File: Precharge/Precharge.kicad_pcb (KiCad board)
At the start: 2 copper layers, 87.1 x 86.1 mm, 62 parts, among them J1 Conn_01x02, J2 Conn_01x02, J3 Molex MicroFit, J4 Conn_02x03_Counter_Clockwise, K1 KT12-1A-40L-THT, Q1 AO3400A, Q2 2N7002, U1 LM393, U2 4N35, U3 4N35, U4 NE555D

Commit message: v2.0
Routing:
- net GLV-: vias 28 -> 29
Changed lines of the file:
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@@
 	)
 	(via
+		(at 154.432 62.23)
+		(size 0.6)
+		(drill 0.3)
+		(layers "F.Cu" "B.Cu")
+		(free yes)
+		(net 2)
+	)
+	(via
 		(at 145.754 96.239)
 		(size 0.6)
@@
 	)
 	(via
-		(at 133.154 107.739)
+		(at 133.096 106.426)
 		(size 0.6)
 		(drill 0.3)
@@
 	)
 	(via
-		(at 133.279 105.989)
+		(at 133.279 100.33)
 		(size 0.6)
 		(drill 0.3)
@@
 	)
 	(segment
-		(start 117.9576 84.5926)
+		(start 117.379 84.014)
 		(end 116.673 83.308)
 		(width 0.635)
@@
 	)
 	(segment
-		(start 117.9576 102.2604)
-		(end 117.9576 84.5926)
-		(width 0.635)
-		(layer "F.Cu")
-		(net 36)
-	)
-	(segment
 		(start 113.03 79.315)
 		(end 112.979 79.264)
@@
 	(segment
 		(start 117.348 102.87)
-		(end 117.9576 102.2604)
+		(end 117.379 102.839)
 		(width 0.635)
 		(layer "F.Cu")
@@
 	)
 	(segment
+		(start 117.379 102.839)
+		(end 117.379 84.014)
+		(width 0.635)
+		(layer "F.Cu")
+		(net 36)
+	)
+	(segment
 		(start 74.1172 92.1512)
 		(end 74.1172 72.4408)
@@
 		(polygon
 			(pts
-				(xy 157.229 51.239) (xy 133.204 51.439) (xy 132.779 137.489) (xy 157.229 137.464)
+				(xy 156.467 58.859) (xy 131.813 58.984) (xy 131.763 128.345) (xy 156.467 128.32)
 			)
 		)

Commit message: v2.1
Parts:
- added Q3: 2N7002, Package_TO_SOT_SMD:SOT-23, F.Cu at (139.0, 96.3)
- added R29: 1M, Resistor_SMD:R_0603_1608Metric_Pad0.98x0.95mm_HandSolder, F.Cu at (150.1, 89.2)
- R8: value 120 -> 150
- moved R26 13.8 mm to (138.2, 85.0), turned to -90 degrees
- moved R27 8.28 mm to (138.5, 91.2), turned to 90 degrees
- moved R27 7.57 mm to (147.8, 84.9), turned to 90 degrees
- moved R23 5.09 mm to (132.6, 84.8)
- moved C2 4.18 mm to (145.8, 84.9)
- moved R24 4.10 mm to (143.9, 84.9)
- moved R28 4.09 mm to (150.1, 84.9), turned to 90 degrees
- moved C5 1.96 mm to (150.1, 93.2)
- moved G*** 1.59 mm to (109.6, 133.3)
- moved Q1 1.23 mm to (149.6, 98.2), turned to 90 degrees
- moved Q2 0.81 mm to (135.4, 84.6)
- moved R25 0.30 mm to (140.0, 84.9), turned to 90 degrees
- moved R22 0.11 mm to (141.8, 85.0), turned to -90 degrees
- renumbered D7 to D1, D1 to D2, D2 to D3, D6 to D4, D3 to D5, D5 to D6, D4 to D7, R28 to R18, R29 to R19, R18 to R20, R19 to R21, R20 to R22, R21 to R23, R22 to R24, R23 to R25, R24 to R26, R25 to R27, R26 to R28
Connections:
- net Net-(R15-Pad2) renamed /Precharge_12V
- C2 pad 2: GLV- -> Net-(Q3-D)
- C3 pad 2: GLV- -> Net-(Q3-D)
- C4 pad 2: GLV- -> Net-(Q3-D)
- C5 pad 2: GLV- -> Net-(Q3-D)
- R24 pad 1: GLV- -> Net-(Q3-D)
- U1 pad 5: unconnected-(U1B-+-Pad5) -> (no net)
- U1 pad 6: unconnected-(U1B---Pad6) -> (no net)
- U1 pad 7: unconnected-(U1-Pad7) -> (no net)
- U4 pad 1: GLV- -> Net-(Q3-D)
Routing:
- net HV-: track 110.8 -> 194.4 mm, vias 150 -> 217
- net Net-(Q3-D): track 0.00 -> 45.9 mm
- net /Precharge_12V: track 6.34 -> 34.3 mm, vias 0 -> 1
- net /PreCh_Int: track 47.4 -> 67.4 mm, vias 3 -> 2
- net Net-(U4-DIS): track 28.6 -> 15.9 mm
- net Net-(D2-A): track 20.0 -> 9.80 mm
- net /AIR+_Con: track 87.9 -> 81.7 mm
- net Net-(D4-A): track 31.7 -> 26.3 mm
- net GLV-: track 0.26 -> 5.23 mm, vias 29 -> 38
- net /PreCh_Complt: track 61.3 -> 65.1 mm
- net /SDC_IN: track 116.0 -> 113.1 mm, vias 2 -> 0
- net Net-(U4-TR): track 11.3 -> 12.7 mm
- net Net-(U1C-V+): track 17.2 -> 16.0 mm
- net Net-(J2-Pin_2): track 54.7 -> 55.8 mm
- net /AIR+: track 83.3 -> 82.4 mm
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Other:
- board size 87.1 x 86.1 mm -> 85 x 85 mm
- board text added: "0.2000 mm / 0.2000 mm"
- board text added: "0.3000 mm"
- board text added: "1.6000 mm"
- board text added: "2"
- board text added: "85.0372 mm x 85.0344 mm"
- board text added: "BOARD CHARACTERISTICS"
- board text added: "Board Thickness:"
- board text added: "Board overall dimensions:"
- board text added: "Castellated pads:"
- board text added: "Copper Finish:"
- board text added: "Copper Layer Count:"
- board text added: "Edge card connectors:"
- board text added: "Impedance Control:"
- board text added: "Min hole diameter:"
- board text added: "Min track/spacing:"
- board text added: "No"
- board text added: "None"
- board text added: "Plated Board Edge:"
- board text added: "v2.1"
- board text removed: "v2.0"

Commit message: v2.1
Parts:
- Q3: value 2N7002 -> AO3400A
- R27: value 1M -> 10K
- moved D6 5.03 mm to (144.6, 71.2)
- moved D7 4.97 mm to (139.6, 71.1)
- moved REF** 0.20 mm to (84.8, 76.1)
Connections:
- net Net-(U1-Pad1) renamed /Comp_Out
- R27 pad 1: Net-(U4-DIS) -> /SDC_IN
- R27 pad 2: GLV- -> Net-(U4-TR)
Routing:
- net /SDC_IN: track 113.1 -> 119.1 mm
- net /AIR+_Con: track 81.7 -> 78.3 mm
- net Net-(U4-DIS): track 15.9 -> 12.9 mm
- net Net-(U4-TR): track 12.7 -> 15.5 mm
- net Net-(D4-A): track 26.3 -> 29.0 mm
- net Net-(D3-A): track 7.97 -> 6.23 mm
- net Net-(Q3-D): track 45.9 -> 44.9 mm
- net GLV-: vias 38 -> 37

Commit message: v3.0 coming up
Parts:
- removed C3: 0.01uF, Capacitor_SMD:C_0603_1608Metric_Pad1.08x0.95mm_HandSolder
- removed C4: 0.1uF, Capacitor_SMD:C_0603_1608Metric_Pad1.08x0.95mm_HandSolder
- removed C5: 10uF, Resistor_SMD:R_0805_2012Metric_Pad1.20x1.40mm_HandSolder
- removed D7: 1N5819, Diode_THT:D_DO-41_SOD81_P7.62mm_Horizontal
- removed R24, R29: 1M, Resistor_SMD:R_0603_1608Metric_Pad0.98x0.95mm_HandSolder
- removed R27 (x2): 10K, Resistor_SMD:R_0603_1608Metric_Pad0.98x0.95mm_HandSolder
- removed R28: 220K, Resistor_SMD:R_0603_1608Metric_Pad0.98x0.95mm_HandSolder
- removed REF**: Symbol_HighVoltage_Triangle_6x6mm_Copper, Symbol:Symbol_HighVoltage_Triangle_6x6mm_Copper
- removed U4: NE555D, Package_SO:SOIC-8_3.9x4.9mm_P1.27mm
- added 2.7M1: R, Resistor_SMD:R_0603_1608Metric_Pad0.98x0.95mm_HandSolder, F.Cu at (163.0, 87.5)
- C2: value 0.1uF -> 6.8uF; footprint Capacitor_SMD:C_0603_1608Metric_Pad1.08x0.95mm_HandSolder -> Capacitor_SMD:C_0805_2012Metric_Pad1.18x1.45mm_HandSolder
- D1: value M7 -> 1n4937; footprint Diode_SMD:D_SMA_Handsoldering -> Diode_THT:D_DO-41_SOD81_P7.62mm_Horizontal
- D2: value 1N5819 -> 1n4937
- Q2: value 2N7002 -> AO3400A
- moved D1 4.76 mm to (113.0, 72.0)
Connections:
- C2 pad 1: Net-(U4-TR) -> Net-(Q3-G)
- C2 pad 2: Net-(Q3-D) -> GLV-
- D5 pad 1: Net-(D5-K) -> Net-(D4-A)
- Q3 pad 1: /Precharge_12V -> Net-(Q3-G)
- Q3 pad 3: Net-(Q3-D) -> Net-(D4-A)
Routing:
- net (no net): track 0.00 -> 59.9 mm
- net Net-(Q3-D): track 44.9 -> 0.00 mm
- net Net-(D5-K): track 41.6 -> 0.00 mm, vias 2 -> 0
- net Net-(D4-A): track 29.0 -> 70.6 mm, vias 0 -> 2
- net HV-: track 194.4 -> 211.2 mm
- net Net-(U4-TR): track 15.5 -> 0.00 mm
- net Net-(Q3-G): track 0.00 -> 15.5 mm
- net Net-(U4-DIS): track 12.9 -> 0.00 mm
- net Net-(D1-A): track 27.6 -> 30.4 mm
- net Net-(U4-CV): track 2.18 -> 0.00 mm
- net Net-(D1-K): track 8.81 -> 9.77 mm

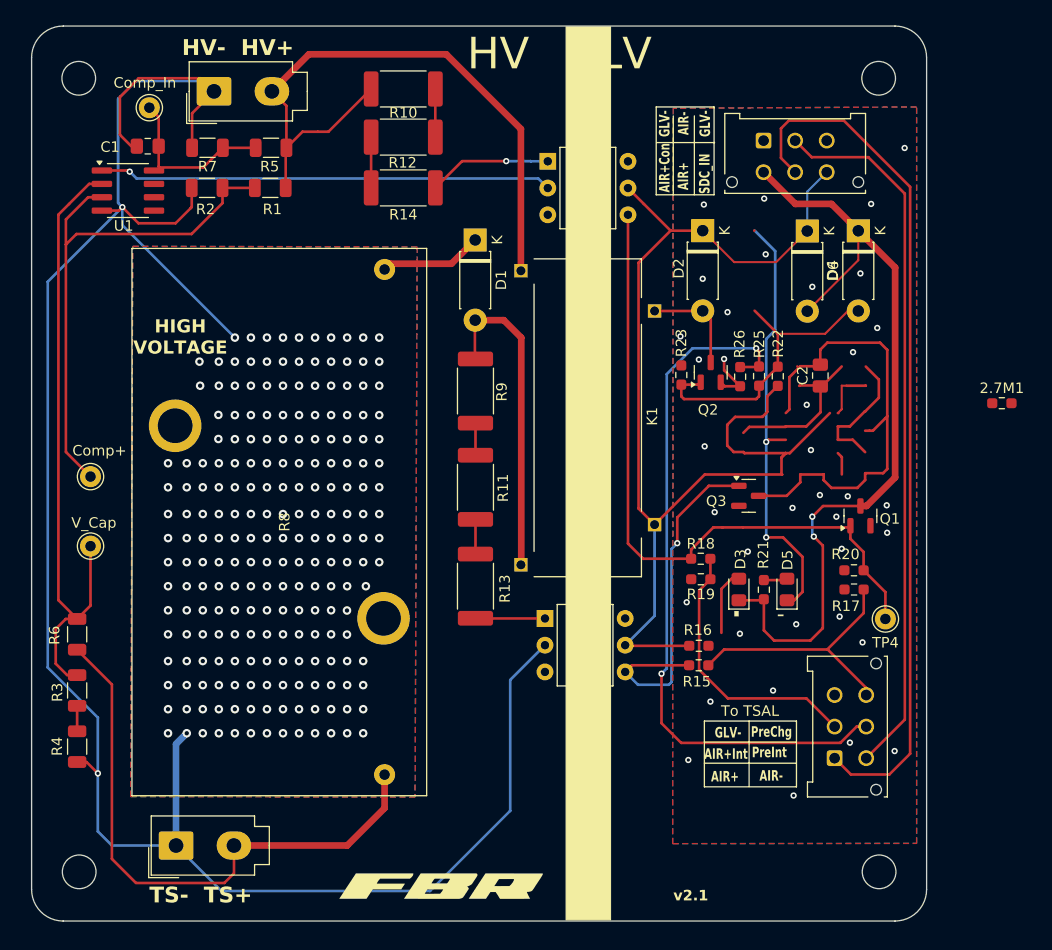
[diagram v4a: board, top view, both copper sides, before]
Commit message: ADD TSAL boards and MOD Precharge
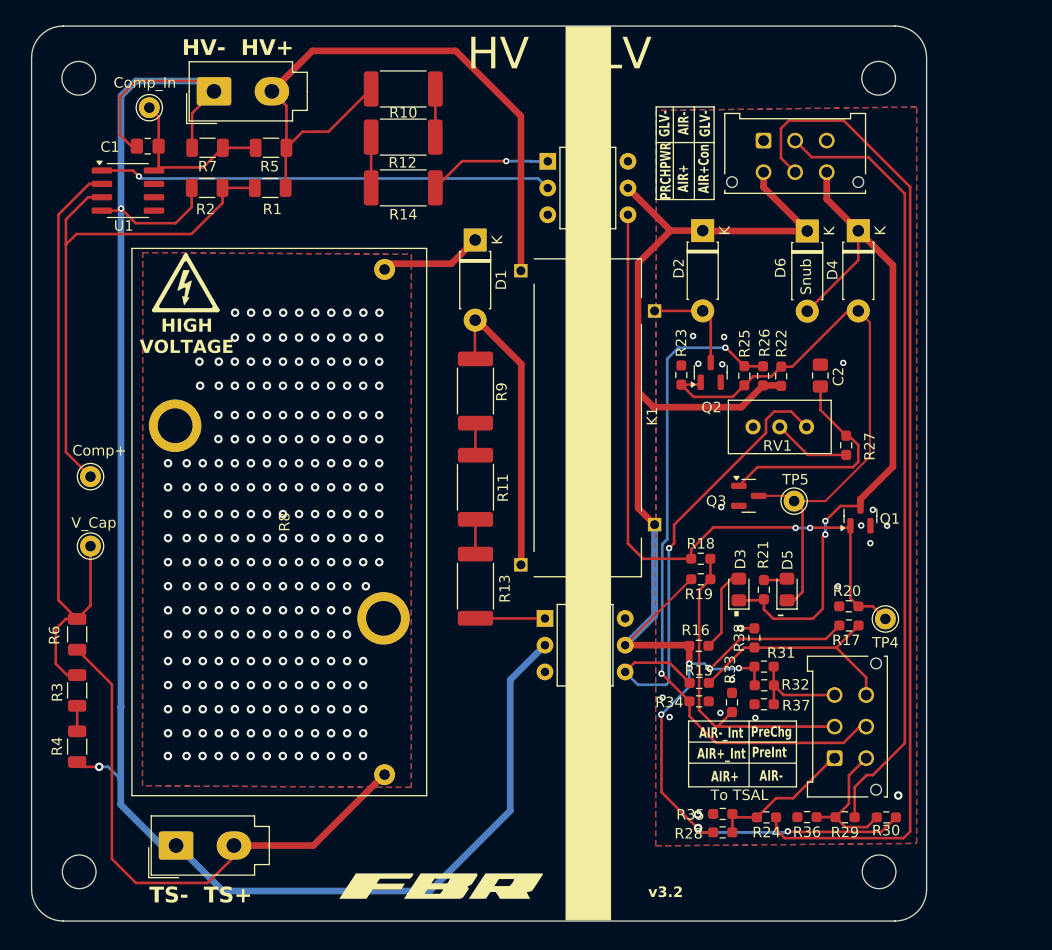
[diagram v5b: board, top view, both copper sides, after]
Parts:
- removed 2.7M1: R, Resistor_SMD:R_0603_1608Metric_Pad0.98x0.95mm_HandSolder
- added R24: 34.8K, Resistor_SMD:R_0603_1608Metric_Pad0.98x0.95mm_HandSolder, F.Cu at (140.7, 126.9)
- added R27: 1.8Meg, Resistor_SMD:R_0603_1608Metric_Pad0.98x0.95mm_HandSolder, F.Cu at (148.3, 91.5)
- added R28: 75K, Resistor_SMD:R_0603_1608Metric_Pad0.98x0.95mm_HandSolder, F.Cu at (136.5, 128.3)
- added R29: 34.8K, Resistor_SMD:R_0603_1608Metric_Pad0.98x0.95mm_HandSolder, F.Cu at (148.1, 126.9)
- added R30: 75K, Resistor_SMD:R_0603_1608Metric_Pad0.98x0.95mm_HandSolder, F.Cu at (152.1, 126.9)
- added R31: 34.8K, Resistor_SMD:R_0603_1608Metric_Pad0.98x0.95mm_HandSolder, F.Cu at (140.4, 112.5)
- added R32: 75K, Resistor_SMD:R_0603_1608Metric_Pad0.98x0.95mm_HandSolder, F.Cu at (140.5, 114.3)
- added R33: 11K, Resistor_SMD:R_0603_1608Metric_Pad0.98x0.95mm_HandSolder, F.Cu at (137.4, 116.0)
- added R34: 11K, Resistor_SMD:R_0603_1608Metric_Pad0.98x0.95mm_HandSolder, F.Cu at (134.3, 115.8)
- added R35: 11K, Resistor_SMD:R_0603_1608Metric_Pad0.98x0.95mm_HandSolder, F.Cu at (136.5, 126.5)
- added R36: 11K, Resistor_SMD:R_0603_1608Metric_Pad0.98x0.95mm_HandSolder, F.Cu at (144.5, 126.8)
- added R37: 11K, Resistor_SMD:R_0603_1608Metric_Pad0.98x0.95mm_HandSolder, F.Cu at (140.5, 116.1)
- added R38: 11K, Resistor_SMD:R_0603_1608Metric_Pad0.98x0.95mm_HandSolder, F.Cu at (139.5, 109.8)
- added REF**: Symbol_HighVoltage_Triangle_6x6mm_Copper, Symbol:Symbol_HighVoltage_Triangle_6x6mm_Copper, F.Cu at (85.5, 76.1)
- added RV1: R_Potentiometer_Trim, Potentiometer_THT:Potentiometer_Bourns_3296W_Vertical, F.Cu at (144.5, 89.8)
- added TP5: Prech_Shut, Connector_Pin:Pin_D1.0mm_L10.0mm, F.Cu at (143.3, 96.8)
- C2: value 6.8uF -> 10uF
- R1, R6: value 270K -> 330K
- R15: value 6.8K -> 34.8K
- R17: value 4.7K -> 75K
- R18, R25: value 33K -> 34.8K
- R19, R26: value 22K -> 75K
- R2, R3: value 12K -> 10K
- R4: value 330 -> 270
- moved R20 3.46 mm to (148.5, 106.8)
- moved R17 3.46 mm to (148.5, 108.6), turned to 0 degrees
- moved R26 2.18 mm to (140.4, 84.9), turned to 90 degrees
- moved R15 1.68 mm to (134.3, 114.1), turned to 0 degrees
- moved R25 1.40 mm to (138.6, 84.9)
- moved R22 0.33 mm to (142.1, 85.0)
- turned R19 to 0 degrees
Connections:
- D2 pad 1: /SDC_IN -> /PRECH_PWR
- D6 pad 1: /SDC_IN -> /PRECH_PWR
- J3 pad 2: /AIR- -> /AIR-_Out
- J3 pad 4: /AIR+_Con -> /PRECH_PWR
- J3 pad 5: /AIR+ -> /AIR+_Out
- J3 pad 6: /SDC_IN -> /AIR+_Con
- J4 pad 3: GLV- -> /AIR-_Int
- K1 pad COIL2: /SDC_IN -> /PRECH_PWR
- R15 pad 1: /Precharge -> /Precharge_12V
- R15 pad 2: /Precharge_12V -> /Precharge
- R16 pad 2: /SDC_IN -> /PRECH_PWR
- R17 pad 1: /Precharge -> /PRECH_PWR
- R17 pad 2: GLV- -> /Precharge
- R19 pad 1: /AIR+_Int -> /PRECH_PWR
- R19 pad 2: GLV- -> /AIR+_Int
- R22 pad 2: /SDC_IN -> /PRECH_PWR
- R26 pad 1: /PreCh_Int -> /PRECH_PWR
- R26 pad 2: GLV- -> /PreCh_Int
- U2 pad 5: /SDC_IN -> /PRECH_PWR
- U3 pad 5: /SDC_IN -> /PRECH_PWR
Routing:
- net /PRECH_PWR: track 0.00 -> 162.4 mm, vias 0 -> 6
- net /SDC_IN: track 119.1 -> 0.00 mm
- net /AIR+_Out: track 0.00 -> 95.6 mm
- net /AIR-_Out: track 0.00 -> 74.1 mm
- net /AIR+: track 82.4 -> 13.9 mm
- net (no net): track 59.9 -> 0.00 mm
- net /AIR-: track 67.7 -> 13.3 mm
- net HV-: track 211.2 -> 176.3 mm, vias 217 -> 240
- net /Precharge_12V: track 34.3 -> 45.8 mm
- net /AIR+_Con: track 78.3 -> 67.5 mm
- net Net-(D4-A): track 70.6 -> 60.2 mm, vias 2 -> 0
- net /AIR-_Int: track 0.00 -> 9.99 mm
- net Net-(R27-Pad1): track 0.00 -> 7.41 mm
- net Net-(Q3-G): track 15.5 -> 21.6 mm
- net /AIR+_Int: track 26.1 -> 30.5 mm
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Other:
- board text added: "AIR+_Int"
- board text added: "AIR-_Int"
- board text added: "HAL SnPb"
- board text added: "PRCHPWR"
- board text added: "Snub"
- board text added: "v3.2"
- board text removed: "AIR+Int"
- board text removed: "None"
- board text removed: "SDC_IN"
- board text removed: "v2.1"

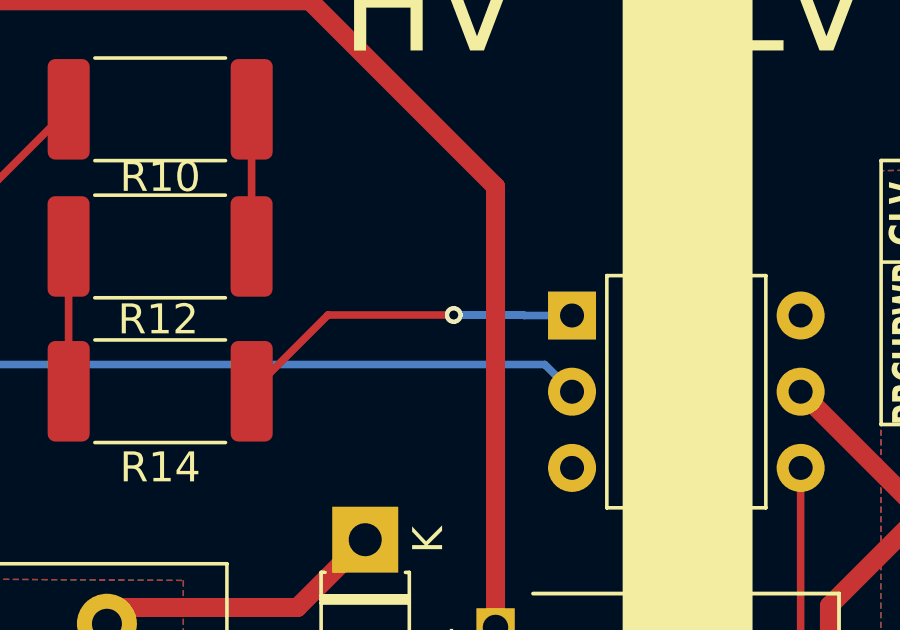
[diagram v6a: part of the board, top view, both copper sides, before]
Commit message: Modify TSAL PCB and use relative paths for libraries
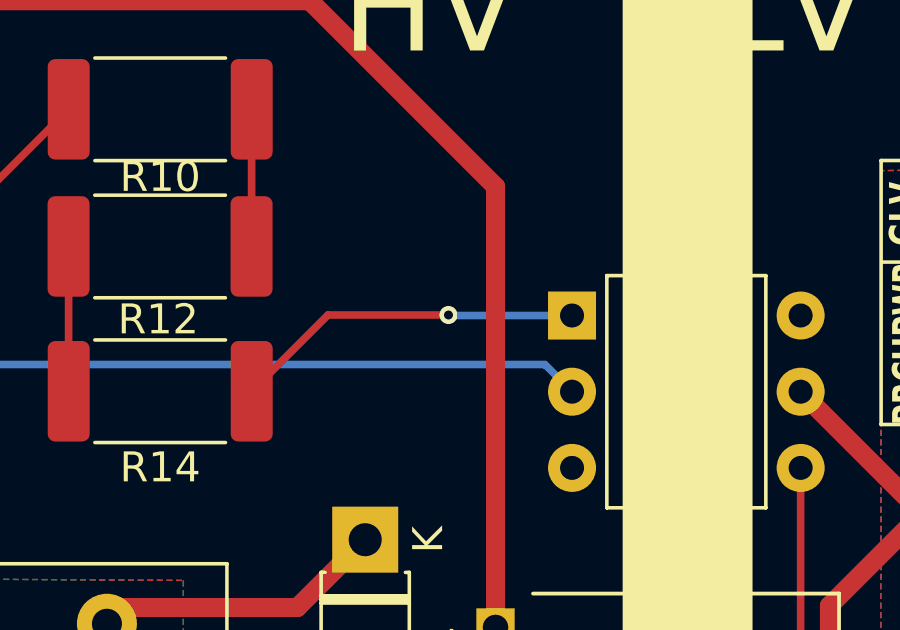
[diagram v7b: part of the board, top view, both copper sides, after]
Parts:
- R15, R18, R24, R29, R31: value 34.8K -> 18K
- R25: value 34.8K -> 7.5K
- R27: value 1.8Meg -> 1.5Meg
- R33, R34, R35, R36, R37, R38: value 11K -> 10K
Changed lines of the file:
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@@
 				(color "White")
 			)
-			(copper_finish "HAL SnPb")
+			(copper_finish "HAL lead-free")
 			(dielectric_constraints no)
 		)
@@
 			)
 		)
-		(property "Value" "11K"
+		(property "Value" "10K"
 			(at 0 1.43 0)
 			(layer "F.Fab")
@@
 			)
 		)
-		(property "Description" "Trim-potentiometer"
+		(property "Description" "Trim-potentiometer 1M Ohm"
 			(at 0 0 0)
 			(unlocked yes)
@@
 			)
 		)
-		(property "Value" "34.8K"
+		(property "Value" "18K"
 			(at 0 1.43 0)
 			(layer "F.Fab")
@@
 			)
 		)
-		(property "Description" "Unpolarized capacitor"
+		(property "Description" "25V Unpolarized capacitor"
 			(at 0 0 90)
 			(unlocked yes)
@@
 			)
 		)
-		(property "Value" "11K"
+		(property "Value" "10K"
 			(at 0 1.43 90)
 			(layer "F.Fab")
@@
 			)
 		)
-		(property "Value" "11K"
+		(property "Value" "10K"
 			(at 0 1.43 0)
 			(layer "F.Fab")
@@
 			)
 		)
-		(property "Value" "34.8K"
+		(property "Value" "18K"
 			(at 0 1.43 0)
 			(layer "F.Fab")
@@
 			)
 		)
-		(property "Value" "11K"
+		(property "Value" "10K"
 			(at 0 1.43 0)
 			(layer "F.Fab")
@@
 			)
 		)
-		(property "Value" "1.8Meg"
+		(property "Value" "1.5Meg"
 			(at 0 1.43 90)
 			(layer "F.Fab")
@@
 			)
 		)
-		(property "Value" "34.8K"
+		(property "Value" "18K"
 			(at 0 1.43 0)
 			(layer "F.Fab")
@@
 			)
 		)
-		(property "Value" "34.8K"
+		(property "Value" "7.5K"
 			(at -3.751 15.1585 90)
 			(layer "F.Fab")
@@
 			)
 		)
-		(property "Value" "11K"
+		(property "Value" "10K"
 			(at 0 1.43 90)
 			(layer "F.Fab")
@@
 			)
 		)
-		(property "Value" "34.8K"
+		(property "Value" "18K"
 			(at 0 1.43 0)
 			(layer "F.Fab")
@@
 			)
 		)
-		(property "Description" ""
+		(property "Description" "Resistor"
 			(at 0 0 90)
 			(unlocked yes)
@@
 			)
 		)
-		(property "Value" "11K"
+		(property "Value" "10K"
 			(at 0 1.43 0)
 			(layer "F.Fab")
@@
 			)
 		)
-		(property "Value" "34.8K"
+		(property "Value" "18K"
 			(at 0 1.43 0)
 			(layer "F.Fab")
@@
 	)
 	(segment
-		(start 115.954 64.514)
+		(start 115.779 64.514)
 		(end 111.762 64.514)
 		(width 0.254)
@@
 	)
 	(via
-		(at 115.954 64.514)
+		(at 115.779 64.514)
 		(size 0.6)
 		(drill 0.3)
@@
 	)
 	(segment
-		(start 118.296 64.531)
-		(end 119.898 64.531)
-		(width 0.254)
-		(layer "B.Cu")
-		(net 31)
-	)
-	(segment
-		(start 118.279 64.514)
-		(end 118.296 64.531)
+		(start 115.779 64.514)
+		(end 115.796 64.531)
 		(width 0.254)
 		(layer "B.Cu")
@@
 	)
 	(segment
-		(start 115.954 64.514)
-		(end 118.279 64.514)
+		(start 115.796 64.531)
+		(end 119.898 64.531)
 		(width 0.254)
 		(layer "B.Cu")

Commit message: minor changes
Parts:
- added R39: 10K, Resistor_SMD:R_0603_1608Metric_Pad0.98x0.95mm_HandSolder, F.Cu at (134.5, 99.2)
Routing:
- net /Precharge_12V: track 45.8 -> 48.0 mm
- net /PreCh_Complt: track 66.2 -> 65.6 mm
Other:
- board text added: "v3.3"
- board text removed: "v3.2"
